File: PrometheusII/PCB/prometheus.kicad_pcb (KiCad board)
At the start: 4 copper layers, 223.5 x 222.3 mm, 240 parts, among them J1 0878311420, J10 Conn_02x02_Odd_Even, J11 Conn_02x02_Odd_Even, J12 Conn_02x08_Odd_Even, J13 Conn_02x08_Odd_Even, J14 Conn_02x08_Odd_Even, J2 Conn_02x08_Odd_Even, J3 Conn_02x02_Odd_Even, J4 Conn_02x02_Odd_Even, J7 Conn_02x08_Odd_Even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

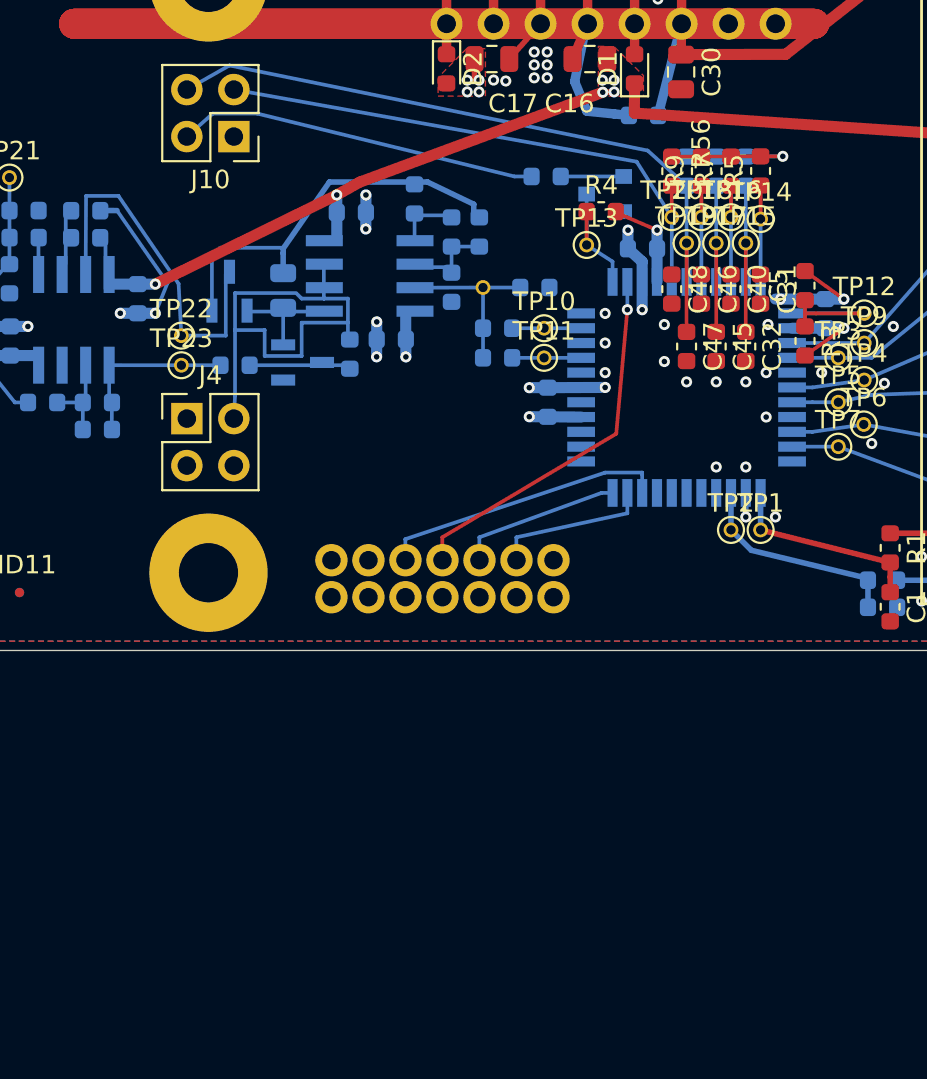
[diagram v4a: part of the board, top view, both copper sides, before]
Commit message: Move switch glitch capacitors to controls board, removed extra filter on ext clk
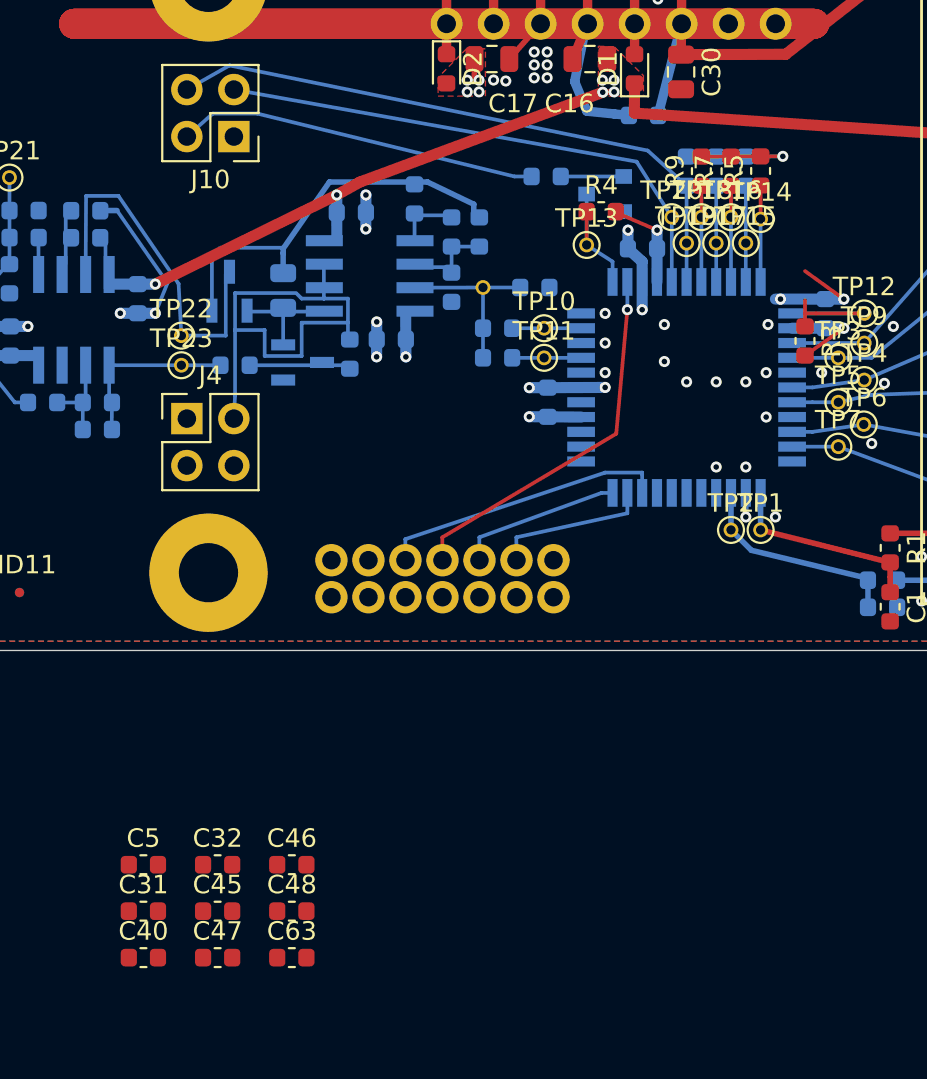
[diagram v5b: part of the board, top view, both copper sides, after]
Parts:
- removed R56: 100k, Resistor_SMD:R_0603_1608Metric
- added C63: 100n, Capacitor_SMD:C_0603_1608Metric, F.Cu at (147.9, 146.0)
- moved C40 48.1 mm to (139.9, 146.0), turned to 0 degrees
- moved C5 47.5 mm to (139.9, 140.9), turned to 0 degrees
- moved C31 47.4 mm to (139.9, 143.5), turned to 0 degrees
- moved C47 41.6 mm to (143.9, 146.0), turned to 0 degrees
- moved C45 40.7 mm to (143.9, 143.5), turned to 0 degrees
- moved C32 40.0 mm to (143.9, 140.9), turned to 0 degrees
- moved C48 39.4 mm to (147.9, 143.5), turned to 0 degrees
- moved C46 38.2 mm to (147.9, 140.9), turned to 0 degrees
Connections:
- C31 pad 1: /VOCT_OCT_A -> /VOCT_OCT_A_P
- C32 pad 1: /POLY_A -> /POLY_A_P
- C40 pad 1: /POLY_B -> /POLY_B_P
- C45 pad 1: /VOCT_SEMI_A -> /VOCT_SEMI_A_P
- C46 pad 1: /VOCT_SEMI_B -> /VOCT_SEMI_A_P
- C47 pad 1: /GLITCH_IN_T -> /GLITCH_EN_P
- C48 pad 1: /EXT_CLK -> /FREQ_LOCK_P
- C5 pad 1: /VOCT_OCT_B -> /VOCT_OCT_B_P
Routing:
- net /VOCT_SEMI_A: track 10.0 -> 5.20 mm
- net /POLY_A: track 10.0 -> 5.20 mm
- net /GLITCH_IN_T: track 38.6 -> 33.8 mm
- net /EXT_CLK: track 30.9 -> 29.2 mm
- net +3V3: track 146.9 -> 145.3 mm

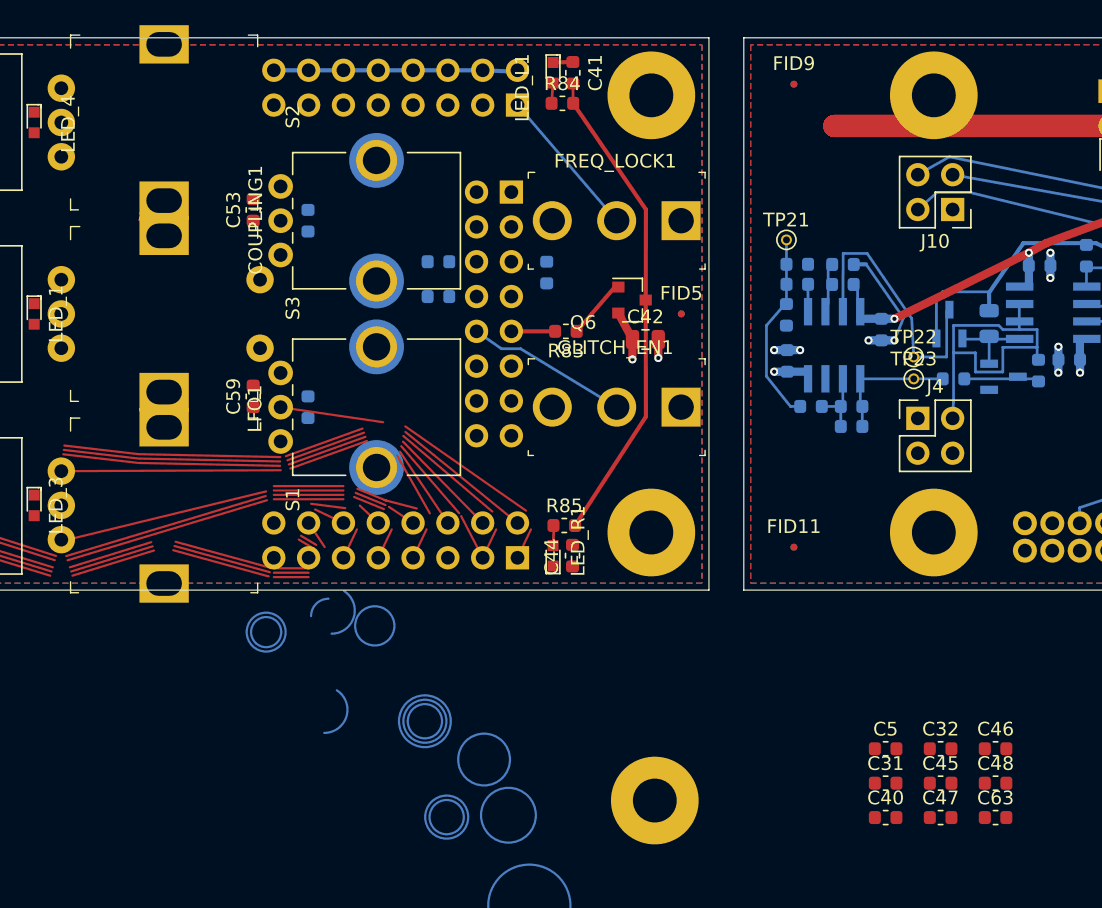
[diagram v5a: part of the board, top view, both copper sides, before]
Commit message: Placed glitch caps on CIB
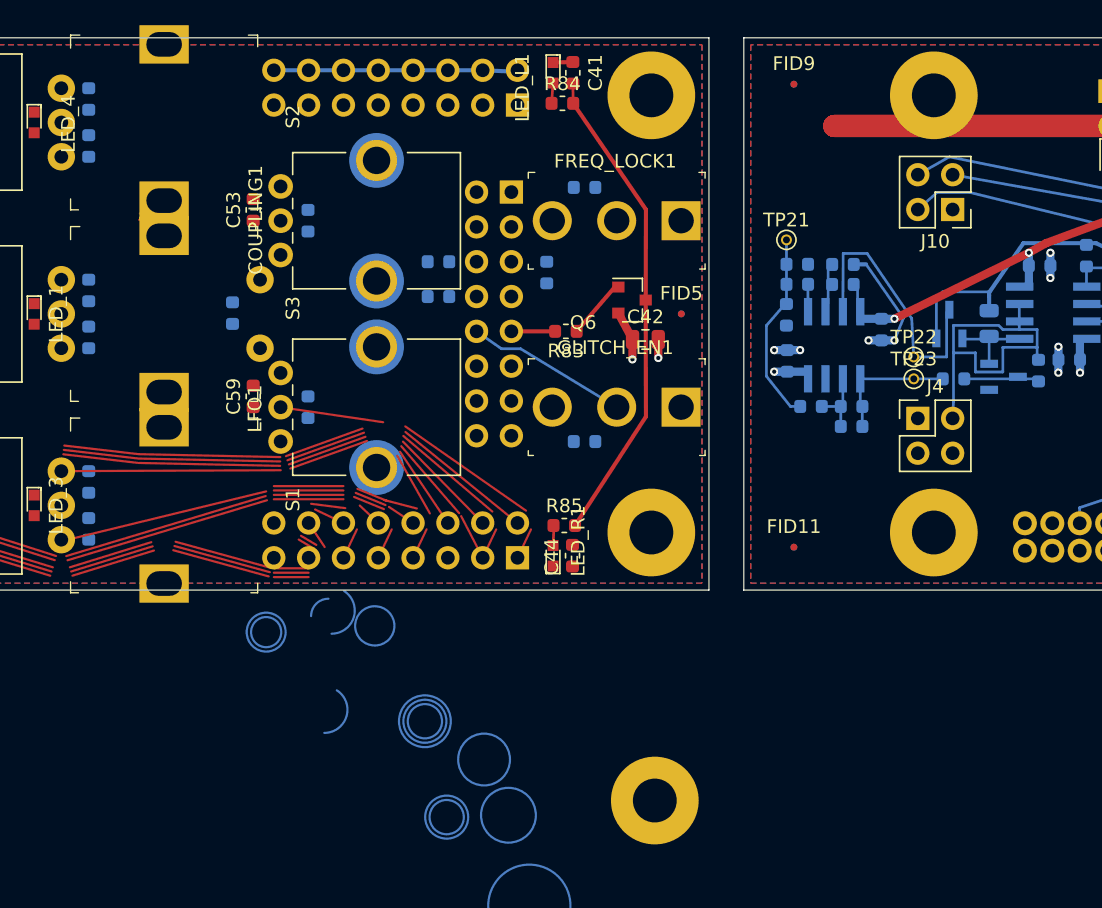
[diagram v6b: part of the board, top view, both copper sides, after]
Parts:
- C31, C32, C40, C45, C46, C47, C48, C5, C63: moved to B.Cu
- moved C45 79.7 mm to (81.7, 93.5), turned to 270 degrees
- moved C46 79.5 mm to (81.7, 97.0), turned to 90 degrees
- moved C32 70.6 mm to (81.7, 107.5), turned to 270 degrees
- moved C40 67.9 mm to (81.7, 110.9), turned to 90 degrees
- moved C63 66.7 mm to (92.2, 109.2), turned to 270 degrees
- moved C31 62.2 mm to (81.7, 121.5), turned to 270 degrees
- moved C5 60.3 mm to (81.7, 124.9), turned to 90 degrees
- moved C48 52.8 mm to (117.9, 100.0), turned to 180 degrees
- moved C47 37.8 mm to (117.9, 118.5), turned to 180 degrees
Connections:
- C46 pad 1: /VOCT_SEMI_A_P -> /VOCT_SEMI_B_P
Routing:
- net /FREQ_LOCK_P: track 11.1 -> 0.00 mm

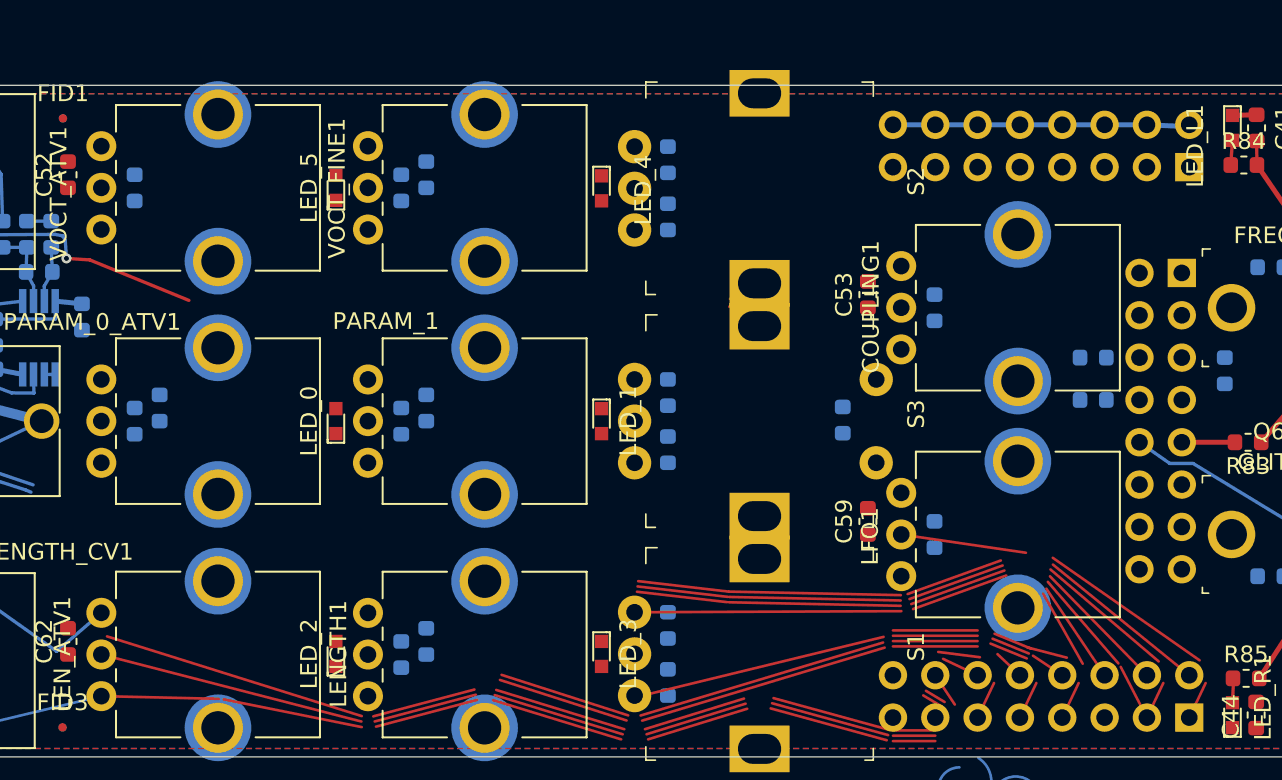
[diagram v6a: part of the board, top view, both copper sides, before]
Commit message: Added net spreading button
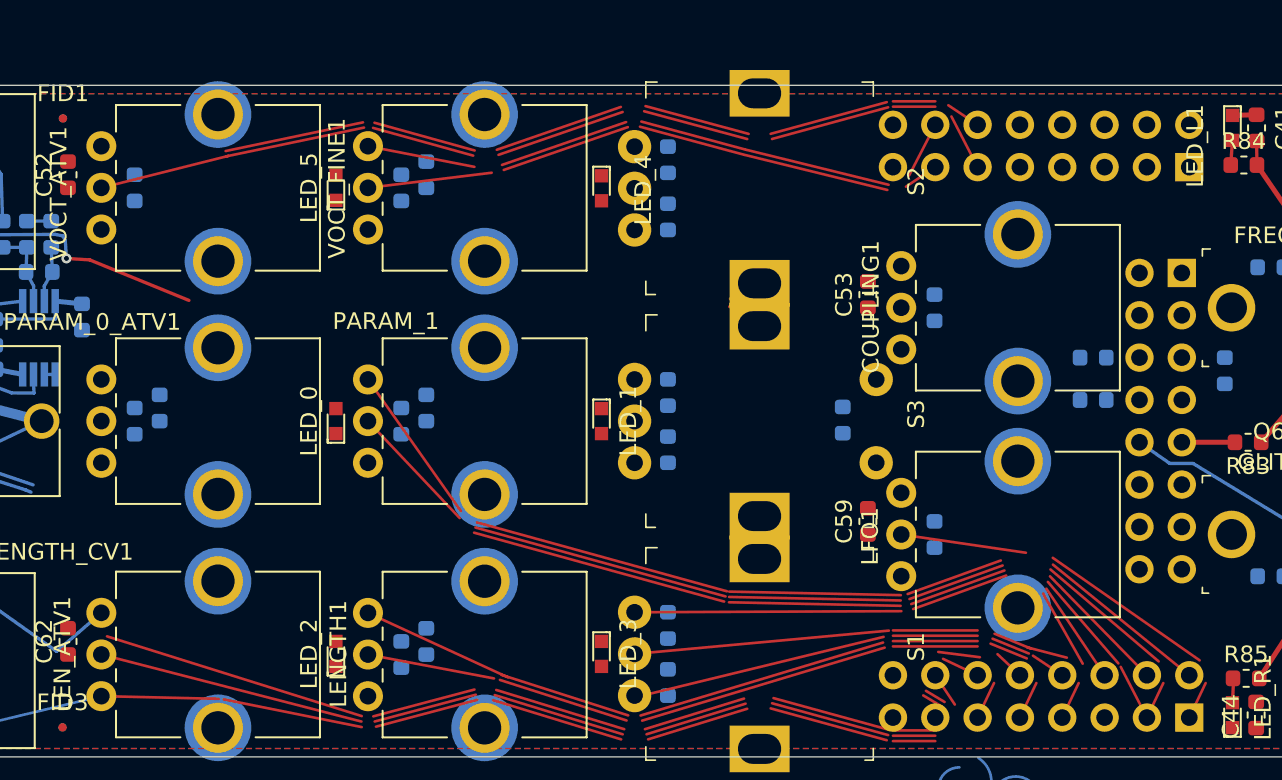
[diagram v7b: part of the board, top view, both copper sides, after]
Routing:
- net GND: track 324.0 -> 475.3 mm
- net (no net): track 514.1 -> 413.6 mm
- net /VOCT_ATV_P: track 0.00 -> 50.0 mm
- net /LEN_CV_P: track 20.7 -> 59.4 mm
- net /VOCT_FINE_P: track 0.00 -> 32.7 mm
- net /LEN_ATV_P: track 18.4 -> 50.0 mm
- net /PARAM_1_P: track 8.31 -> 16.3 mm
- net /LEN_KNOB_P: track 1.85 -> 9.55 mm
